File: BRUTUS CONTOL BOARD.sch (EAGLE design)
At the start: 42 parts, among them IC1 ATMEGA168PROUND, IC4 74LS595N, IC5 74LS595N, IC6 4021N, IC7 4021N, IC8 74LS14N, Q1 16MHz, X1 5566-16, X2 5566-16, X3 5566-2, X4 5566-6, X5 5566-6, X6 5566-8, X7 5566-4

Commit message: rev1
second commit
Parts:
- removed IC7: 4021N, 40xx:4021N
- removed IC8: 74LS14N, 74xx-us:74LS14N
- removed R22: 10k, adafruit:R-US_0204/2V
- added IC2, IC3: 74LS595N, 74xx-us:74LS595N
- added R14: 10k, adafruit:R-US_0204/2V
- C1, C2: value 22uF -> 10uF
- C4, C5: value 10uF -> 22uF
- IC1: value ATMEGA168PROUND -> 74LS14N; device adafruit:ATMEGA168PROUND -> 74xx-us:74LS14N
- IC4: value 74LS595N -> ATMEGA168PROUND; device 74xx-us:74LS595N -> adafruit:ATMEGA168PROUND
- IC5: value 74LS595N -> 4021N; device 74xx-us:74LS595N -> 40xx:4021N
- R2: value 10k -> 220
- R3: value 220 -> 10k
- X1: value 5566-16 -> 5566-6; device con-molex:5566-16 -> con-molex:5566-6
- X4: value 5566-6 -> 5566-4; device con-molex:5566-6 -> con-molex:5566-4
- X5: value 5566-6 -> 5566-16; device con-molex:5566-6 -> con-molex:5566-16
- X7: value 5566-4 -> 5566-6; device con-molex:5566-4 -> con-molex:5566-6
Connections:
- removed net DIGPIN9: IC1.(PCI1/OC1A/OC1S)PB1, IC8C.O
- new net DIGPIN10: IC1C.O, IC4.(PCI2/SS/OC1B)PB2
- net ANLG1: now also IC4.(PCI9/ADC1)PC1, X7-3.S; no longer IC1.(PCI9/ADC1)PC1, X4-3.S
- net ANLG2: now also IC4.(PCI10/ADC2)PC2, X7-4.S; no longer IC1.(PCI10/ADC2)PC2, X4-4.S
- net ANLG3: now also IC4.(PCI11/ADC3)PC3, X7-5.S; no longer IC1.(PCI11/ADC3)PC3, X4-5.S
- net DIGPIN11: now also IC4.(PCI3/MOSI/OC2A)PB3, IC5A.P/!S; no longer IC1.(PCI3/MOSI/OC2A)PB3, IC7A.P/!S
- net DIGPIN12: now also IC4.(PCI4/MISO)PB4, IC5A.CLK; no longer IC1.(PCI4/MISO)PB4, IC7A.CLK
- net DIGPIN2: now also IC1B.O, IC4.(PCI18/INT0)PD2; no longer IC1.(PCI18/INT0)PD2, IC8B.O
- net DIGPIN3: now also IC1A.O, IC4.(PCI19/INT1/OC2B)PD3; no longer IC1.(PCI19/INT1/OC2B)PD3, IC8A.O
- net DIGPIN4: now also IC2A.SER, IC4.(PCI20/XCK/T0)PD4; no longer IC1.(PCI20/XCK/T0)PD4, IC4A.SER
- net DIGPIN5: now also IC2A.RCK, IC3A.RCK, IC4.(PCI21/T1/OC0B)PD5; no longer IC1.(PCI21/T1/OC0B)PD5, IC4A.RCK, IC5A.RCK
- net DIGPIN6: now also IC2A.SCK, IC3A.SCK, IC4.(PCI22/AIN0OC0A)PD6; no longer IC1.(PCI22/AIN0OC0A)PD6, IC4A.SCK, IC5A.SCK
- net DIGPIN7: now also IC4.(PCI23/AIN1)PD7, IC5A.Q8; no longer IC1.(PCI23/AIN1)PD7, IC6A.Q8
- net GND: now also C3.1, C4.2, IC2A.G, IC3A.G, IC4.AGND, IC4.GND, R2.2, X1-2.S, X1-4.S, X4-4.S, X7-6.S; no longer C3.2, C4.1, IC1.AGND, IC1.GND, IC4A.G, IC5A.G, R3.2, X4-6.S, X5-2.S, X5-4.S, X7-4.S
- net IC8A: now also C1.1, IC1A.I, R1.2, X1-1.S; no longer C5.1, IC8A.I, R13.2, X5-1.S
- net IC8B: now also C2.1, IC1B.I, R3.2, X1-3.S; no longer C3.1, IC8B.I, R21.2, X5-3.S
- net IC8C: now also C3.2, IC1C.I, R4.2, X1-5.S; no longer C4.2, IC8C.I, R22.2, X5-5.S
- net N$1: now also C4.1, IC4.PB6(XTAL1/TOSC1/PCI6); no longer C1.1, IC1.PB6(XTAL1/TOSC1/PCI6)
- net N$17: now also IC5A.SI, IC6A.Q8; no longer IC6A.SI, IC7A.Q8
- net N$2: now also C5.1, IC4.PB7(XTAL2/TOSC2/PCI7); no longer C2.1, IC1.PB7(XTAL2/TOSC2/PCI7)
- net N$3: now also IC4.PC6(/RESET/PCI14), R5.2; no longer IC1.PC6(/RESET/PCI14), R1.2
- net N$5: now also IC4.(PCI5/SCK)PB5; no longer IC1.(PCI5/SCK)PB5
- net N$6: now also R2.1; no longer R3.1
- net N$7: now also IC2A.QH*, IC3A.SER; no longer IC4A.QH*, IC5A.SER
- net SCL: now also IC4.(PCI13/ADC5/SCL)PC5, X4-3.S; no longer IC1.(PCI13/ADC5/SCL)PC5, X7-3.S
- net SDA: now also IC4.(PCI12/ADC4/SDA)PC4, X4-2.S; no longer IC1.(PCI12/ADC4/SDA)PC4, X7-2.S
- net VCC: now also IC3A.SCL, IC4.AREF, IC4.AVCC, IC4.VCC, R13.2, R14.1, R17.1, R18.1, R19.1, R21.2, R6.2, R7.2, R9.1; no longer IC1.AREF, IC1.AVCC, IC1.VCC, IC5A.SCL, R13.1, R17.2, R18.2, R19.2, R2.1, R22.1, R6.1, R7.1, R9.2
- net X1-1: now also IC5A.P1, R16.2, X5-1.S; no longer IC6A.P1, R2.2, X1-1.S
- net X1-10: now also IC6A.P2, R21.1, X5-10.S; no longer IC7A.P2, R10.1, X1-10.S
- net X1-11: now also IC6A.P3, R7.1, X5-11.S; no longer IC7A.P3, R12.1, X1-11.S
- net X1-12: now also IC6A.P4, R6.1, X5-12.S; no longer IC7A.P4, R11.1, X1-12.S
- net X1-13: now also R11.1, X5-13.S; no longer R18.1, X1-13.S
- net X1-14: now also IC6A.P6, R10.1, X5-14.S; no longer IC7A.P6, R17.1, X1-14.S
- net X1-15: now also IC6A.P7, R12.1, X5-15.S; no longer IC7A.P7, R19.1, X1-15.S
- net X1-16: now also IC6A.P8, R13.1, X5-16.S; no longer IC7A.P8, R20.1, X1-16.S
- net X1-2: now also IC5A.P2, R15.2, X5-2.S; no longer IC6A.P2, R4.2, X1-2.S
- net X1-3: now also IC5A.P3, R14.2, X5-3.S; no longer IC6A.P3, R5.2, X1-3.S
- net X1-4: now also IC5A.P4, R17.2, X5-4.S; no longer IC6A.P4, R6.2, X1-4.S
- net X1-5: now also IC5A.P5, R18.2, X5-5.S; no longer IC6A.P5, R7.2, X1-5.S
- net X1-6: now also IC5A.P6, R8.2, X5-6.S; no longer IC6A.P6, R15.2, X1-6.S
- net X1-7: now also IC5A.P7, R19.2, X5-7.S; no longer IC6A.P7, R8.2, X1-7.S
- net X1-8: now also IC5A.P8, R9.2, X5-8.S; no longer IC6A.P8, R16.2, X1-8.S
- net X1-9: now also IC6A.P1, R20.1, X5-9.S; no longer IC7A.P1, R9.1, X1-9.S
- net X2-1: now also IC2A.QA; no longer IC4A.QA
- net X2-10: now also IC3A.QB; no longer IC5A.QB
- net X2-11: now also IC3A.QC; no longer IC5A.QC
- net X2-12: now also IC3A.QD; no longer IC5A.QD
- net X2-13: now also IC3A.QE; no longer IC5A.QE
- net X2-14: now also IC3A.QF; no longer IC5A.QF
- net X2-15: now also IC3A.QG; no longer IC5A.QG
- net X2-16: now also IC3A.QH; no longer IC5A.QH
- net X2-2: now also IC2A.QB; no longer IC4A.QB
- net X2-3: now also IC2A.QC; no longer IC4A.QC
- net X2-4: now also IC2A.QD; no longer IC4A.QD
- net X2-5: now also IC2A.QE; no longer IC4A.QE
- net X2-6: now also IC2A.QF; no longer IC4A.QF
- net X2-7: now also IC2A.QG; no longer IC4A.QG
- net X2-8: now also IC2A.QH; no longer IC4A.QH
- net X2-9: now also IC3A.QA; no longer IC5A.QA
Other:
- moved on the sheet: C1, C2, C3, C4, C5, IC6, R1, R10, R11, R12, R13, R15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

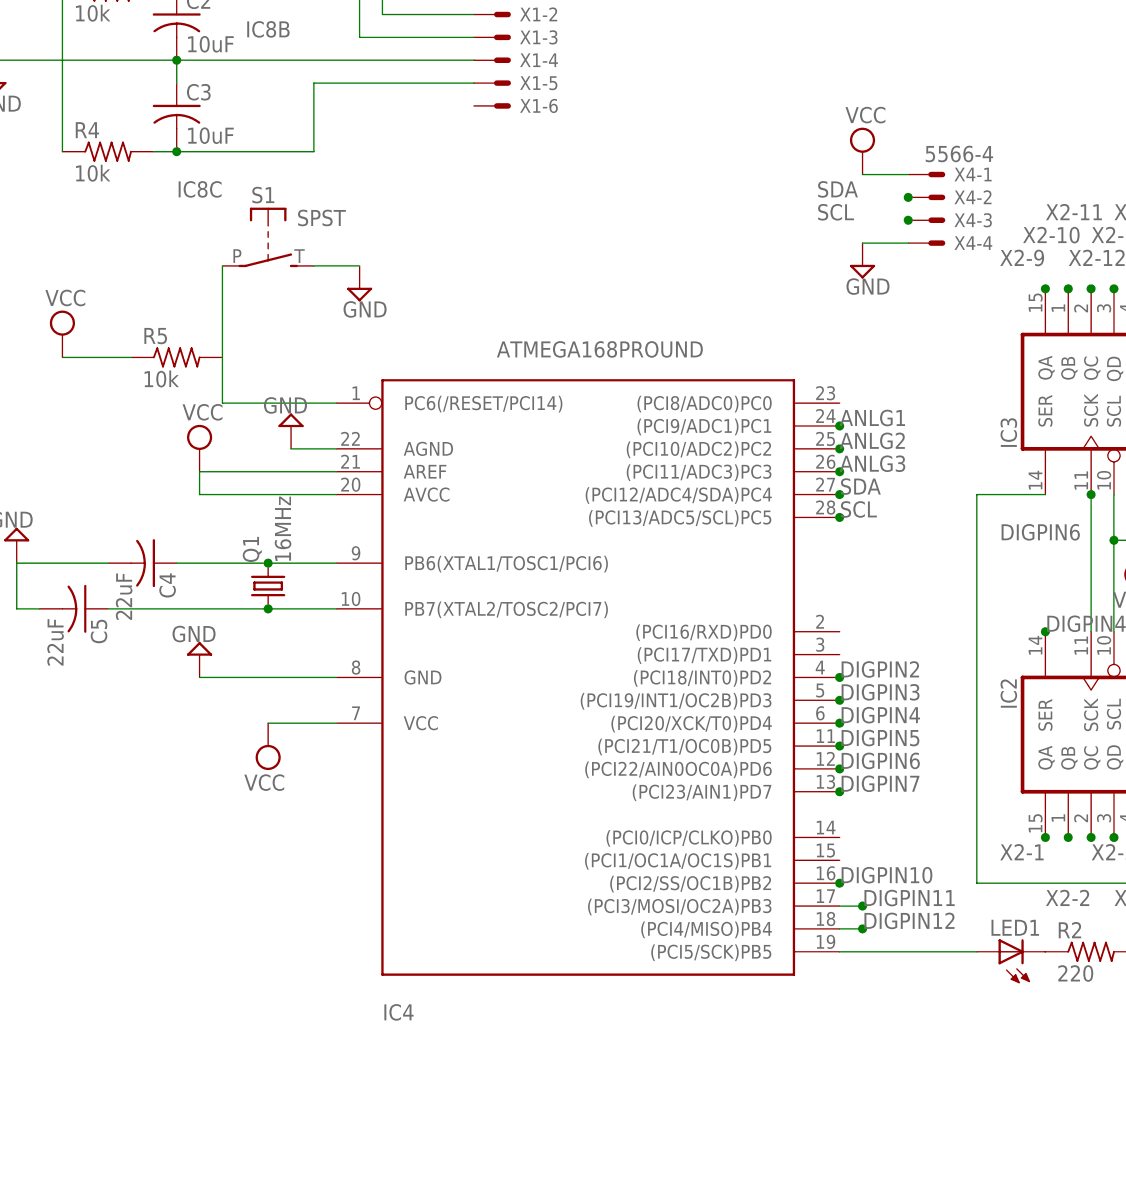
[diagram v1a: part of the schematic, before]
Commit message: REV 2
Changed to IC socket for ATmega328 connection
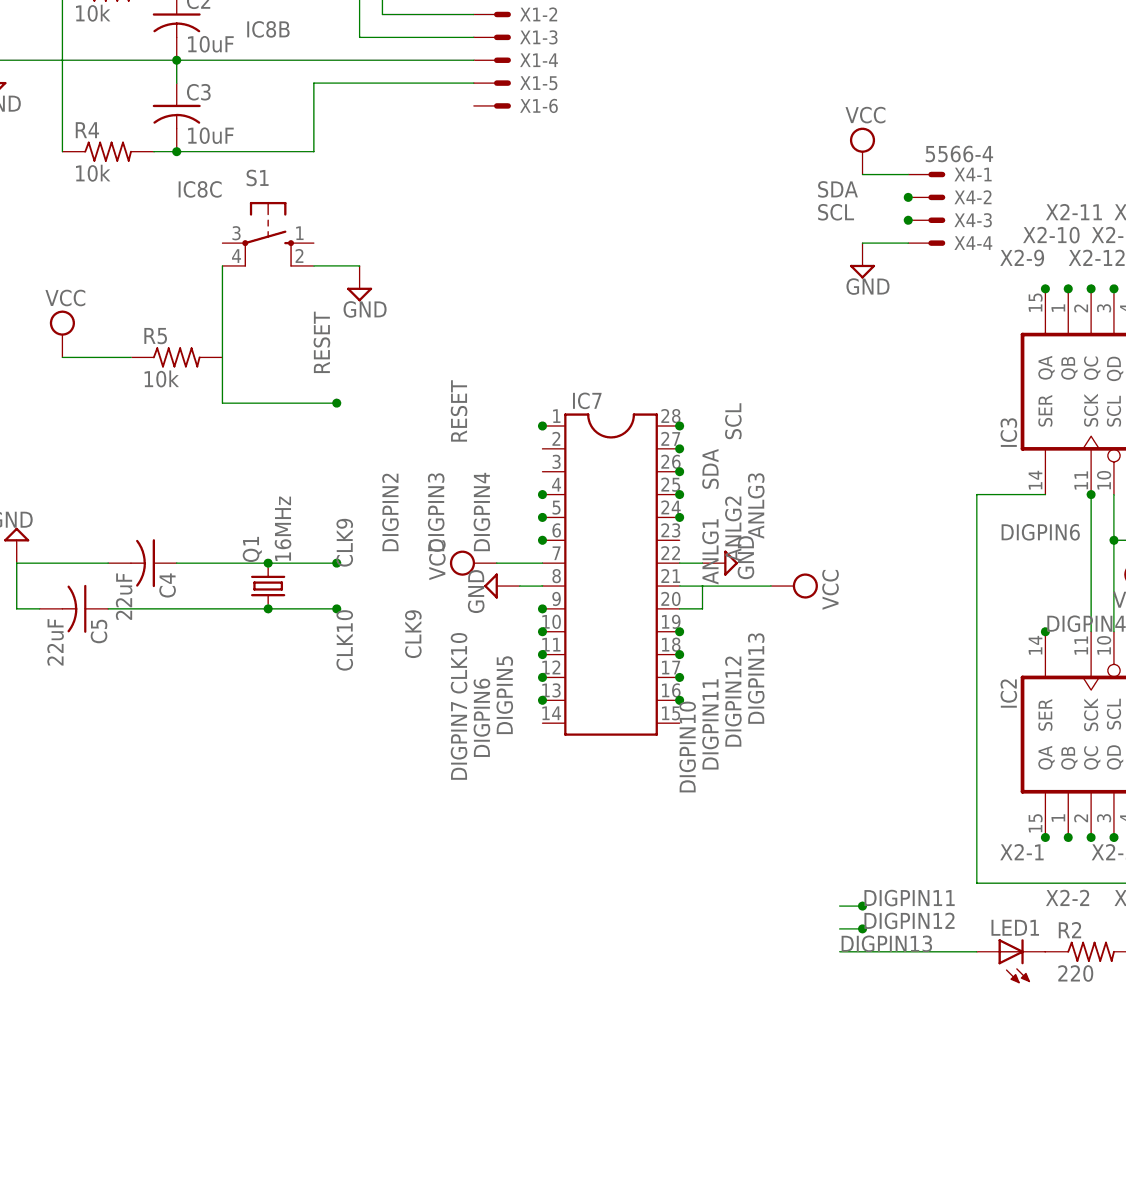
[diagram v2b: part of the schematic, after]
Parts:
- removed IC4: ATMEGA168PROUND, adafruit:ATMEGA168PROUND
- added IC7: (no value), ic-package:DIL28-3
- S1: value SPST -> (none); device adafruit:SPST -> adafruit:40-XX
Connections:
- removed net N$1: C4.1, IC4.PB6(XTAL1/TOSC1/PCI6), Q1.2
- removed net N$2: C5.1, IC4.PB7(XTAL2/TOSC2/PCI7), Q1.1
- removed net N$3: IC4.PC6(/RESET/PCI14), R5.2, S1.P
- removed net N$5: IC4.(PCI5/SCK)PB5, LED1.A
- new net CLK10: C5.1, IC7.10, Q1.1
- new net CLK9: C4.1, IC7.9, Q1.2
- new net DIGPIN13: IC7.19, LED1.A
- new net RESET: IC7.1, R5.2, S1.P1
- net ANLG1: now also IC7.24; no longer IC4.(PCI9/ADC1)PC1
- net ANLG2: now also IC7.25; no longer IC4.(PCI10/ADC2)PC2
- net ANLG3: now also IC7.26; no longer IC4.(PCI11/ADC3)PC3
- net DIGPIN10: now also IC7.16; no longer IC4.(PCI2/SS/OC1B)PB2
- net DIGPIN11: now also IC7.17; no longer IC4.(PCI3/MOSI/OC2A)PB3
- net DIGPIN12: now also IC7.18; no longer IC4.(PCI4/MISO)PB4
- net DIGPIN2: now also IC7.4; no longer IC4.(PCI18/INT0)PD2
- net DIGPIN3: now also IC7.5; no longer IC4.(PCI19/INT1/OC2B)PD3
- net DIGPIN4: now also IC7.6; no longer IC4.(PCI20/XCK/T0)PD4
- net DIGPIN5: now also IC7.11; no longer IC4.(PCI21/T1/OC0B)PD5
- net DIGPIN6: now also IC7.12; no longer IC4.(PCI22/AIN0OC0A)PD6
- net DIGPIN7: now also IC7.13; no longer IC4.(PCI23/AIN1)PD7
- net GND: now also IC7.22, IC7.8, S1.S1; no longer IC4.AGND, IC4.GND, S1.S
- net SCL: now also IC7.28; no longer IC4.(PCI13/ADC5/SCL)PC5
- net SDA: now also IC7.27; no longer IC4.(PCI12/ADC4/SDA)PC4
- net VCC: now also IC7.20, IC7.21, IC7.7; no longer IC4.AREF, IC4.AVCC, IC4.VCC
